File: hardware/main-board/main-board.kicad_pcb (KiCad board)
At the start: 2 copper layers, 176 x 55 mm, 101 parts, among them J1 BARREL_JACK, J2 CONN_01X10, J3 CONN_01X10, J4 USB_OTG, J5 CONN_02X05, J6 SMA, Q1 DDTD113ZC, Q2 DDTD113ZC, Q3 DDTD113ZC, Q4 DDTD113ZC, Q5 DDTD113ZC, Q6 FDB14N30TM, Q7 DDTD113ZC, Q8 DDTD113ZC, Q9 DDTD113ZC, SW1 SW_Push, SW2 SW_Push, SW3 SW_Push, SW4 SW_Push, SW5 SW_DIP_x01, U1 LD1117S33TR, U2 MAX1771, U3 STM32F302C, U4 FGPMMOPA6H, Y1 8MHz, Y2 32.768kHz

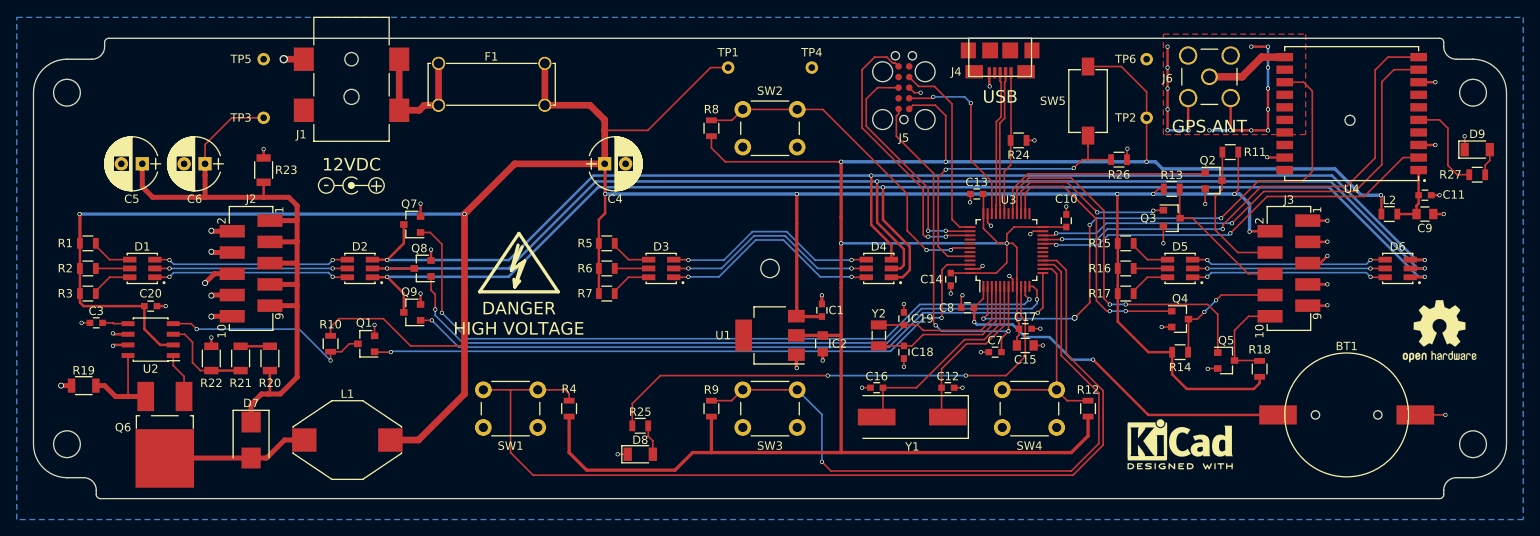
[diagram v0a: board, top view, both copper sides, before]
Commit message: Fixed HV5522 footprint on tube board.  Increased size of IN-14 through holes.  Fixed footprint for MOSFET in HV boost circuit.  Fixed hole size for battery holder footprint.
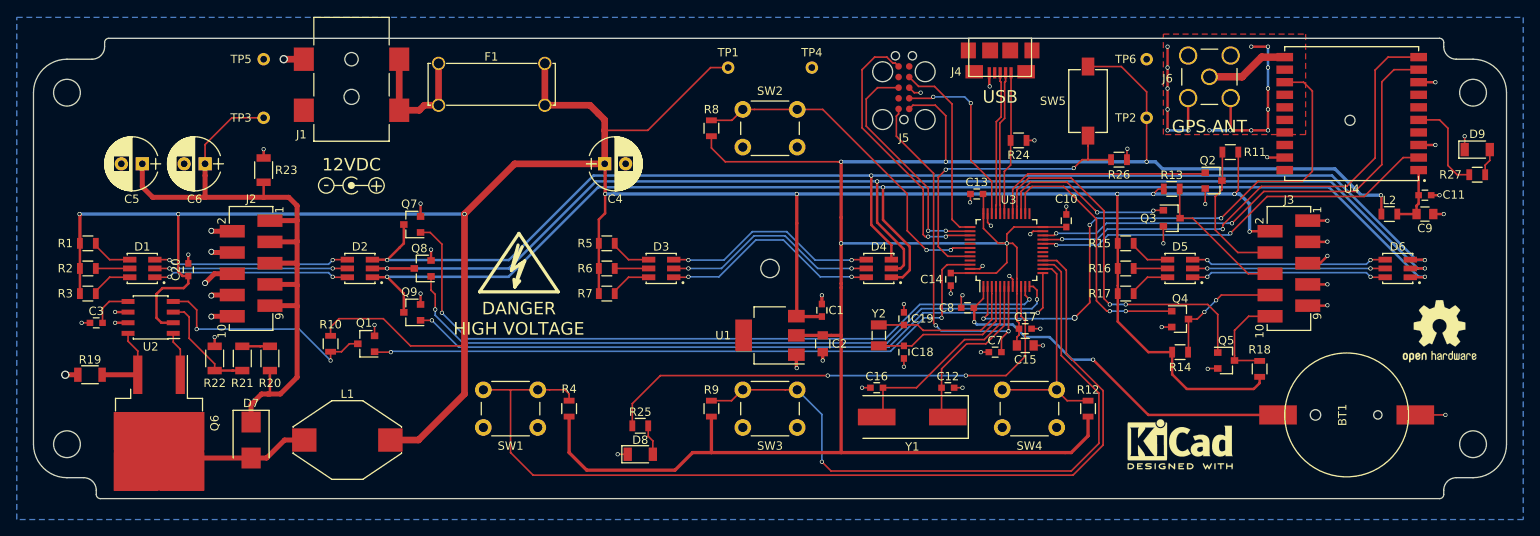
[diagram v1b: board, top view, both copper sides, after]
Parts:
- Q6: footprint TO_SOT_Packages_SMD:TO-252-2Lead -> TO_SOT_Packages_SMD:TO-263-2
- moved C20 6.26 mm to (80.5, 90.2), turned to 90 degrees
- moved U2 2.65 mm to (76.0, 95.8)
- moved R19 1.50 mm to (68.8, 102.7)
- moved Q6 0.88 mm to (77.0, 108.5)
- moved R22 0.40 mm to (83.7, 100.8)
- moved R21 0.20 mm to (87.0, 100.8)
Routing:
- net +12V: track 339.7 -> 342.4 mm, vias 8 -> 9
- net Net-(Q1-Pad3): track 25.3 -> 27.8 mm
- net Net-(C3-Pad1): track 3.09 -> 5.13 mm
- net Net-(R21-Pad2): track 11.3 -> 13.1 mm
- net Net-(Q6-Pad3): track 11.4 -> 9.69 mm
- net Net-(D7-Pad2): track 17.6 -> 16.1 mm

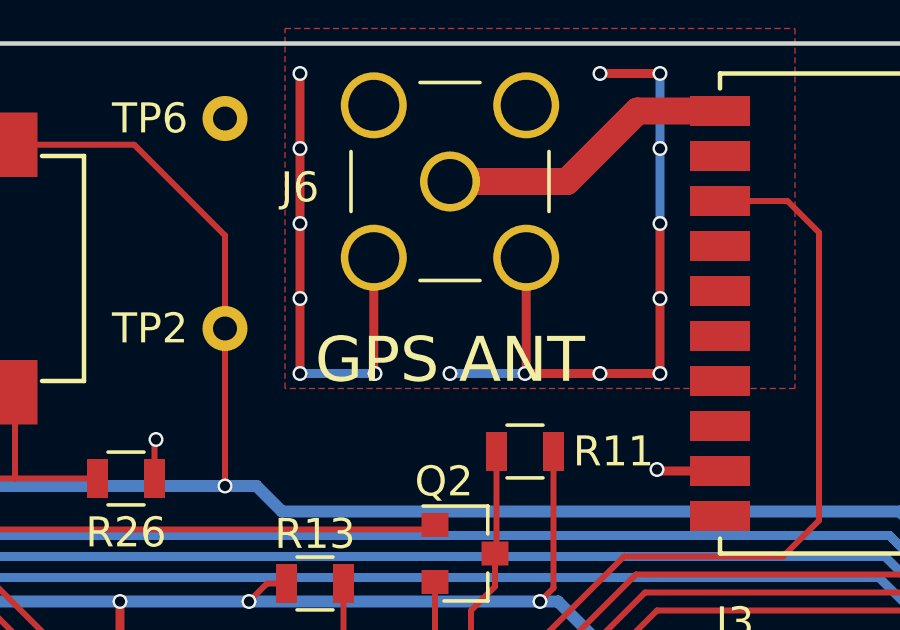
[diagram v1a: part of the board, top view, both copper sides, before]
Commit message: Modified thermal relief on SMA connector
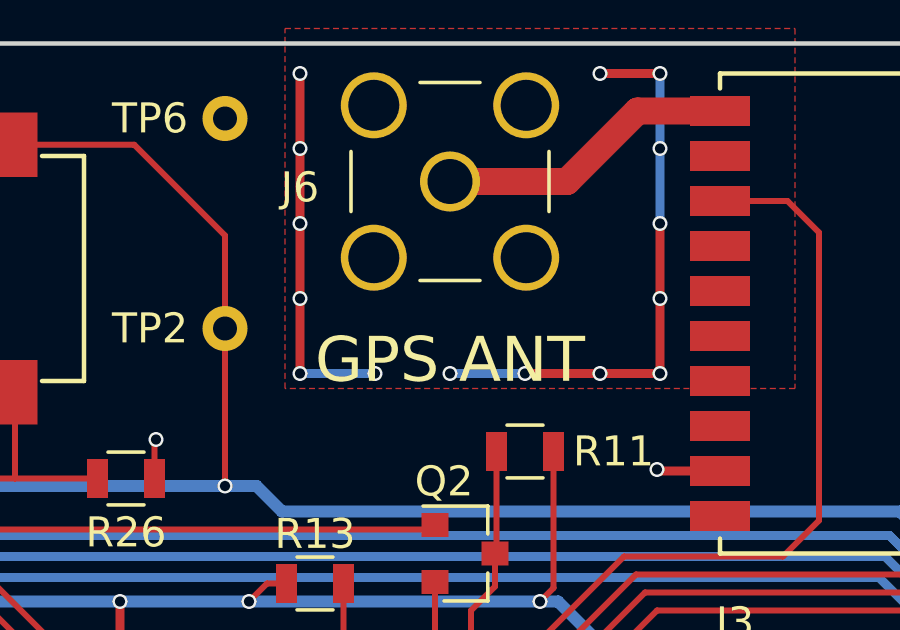
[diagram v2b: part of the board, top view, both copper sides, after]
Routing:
- net GND: track 130.1 -> 122.4 mm
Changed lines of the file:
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@@
     (thickness 1.6)
     (drawings 34)
-    (tracks 950)
+    (tracks 948)
     (zones 0)
     (modules 101)
@@
     (user_trace_width 0.8)
     (trace_clearance 0.2)
-    (zone_clearance 0.5)
+    (zone_clearance 0.16)
     (zone_45_only no)
     (trace_min 0.16)
@@
   (segment (start 205 73.5) (end 202.5 73.5) (width 0.3) (layer B.Cu) (net 1))
   (via (at 202.5 73.5) (size 0.5) (drill 0.34) (layers F.Cu B.Cu) (net 1))
-  (segment (start 205.04 69.64) (end 205.04 73.46) (width 0.3) (layer F.Cu) (net 1))
   (segment (start 205.04 73.46) (end 205 73.5) (width 0.3) (layer F.Cu) (net 1))
   (via (at 205 73.5) (size 0.5) (drill 0.34) (layers F.Cu B.Cu) (net 1))
-  (segment (start 199.96 69.64) (end 199.96 73.46) (width 0.3) (layer F.Cu) (net 1))
   (segment (start 199.96 73.46) (end 200 73.5) (width 0.3) (layer F.Cu) (net 1))
   (via (at 200 73.5) (size 0.5) (drill 0.34) (layers F.Cu B.Cu) (net 1))
@@
     (connect_pads (clearance 0.16))
     (min_thickness 0.2)
-    (fill yes (arc_segments 16) (thermal_gap 0.22) (thermal_bridge_width 0.4) (smoothing fillet) (radius 0.5))
+    (fill yes (arc_segments 16) (thermal_gap 0.4) (thermal_bridge_width 0.3) (smoothing fillet) (radius 0.2))
     (polygon
       (pts

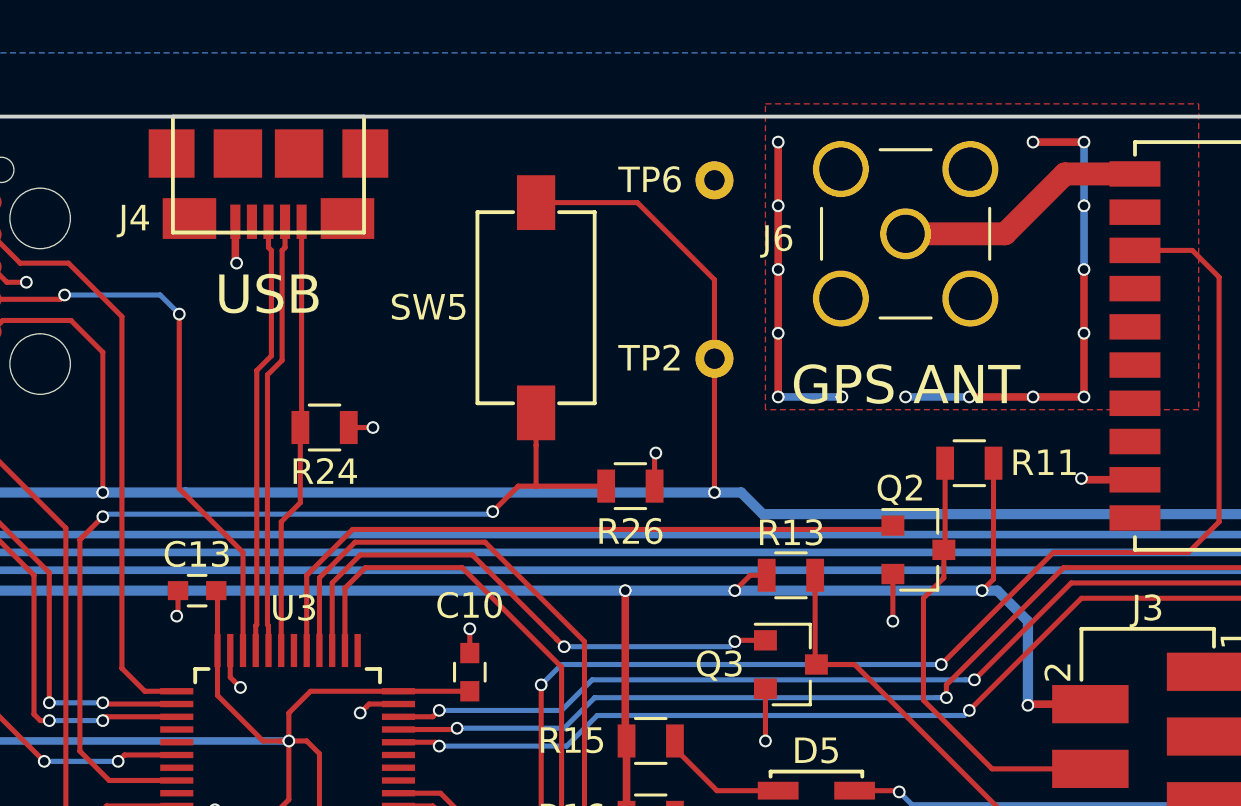
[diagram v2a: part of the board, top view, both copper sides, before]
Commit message: Added pull up circuit for USB.  Changed boot switch to a right angle pushbutton so that it can be used to switch to bootloader mode within the enclosure
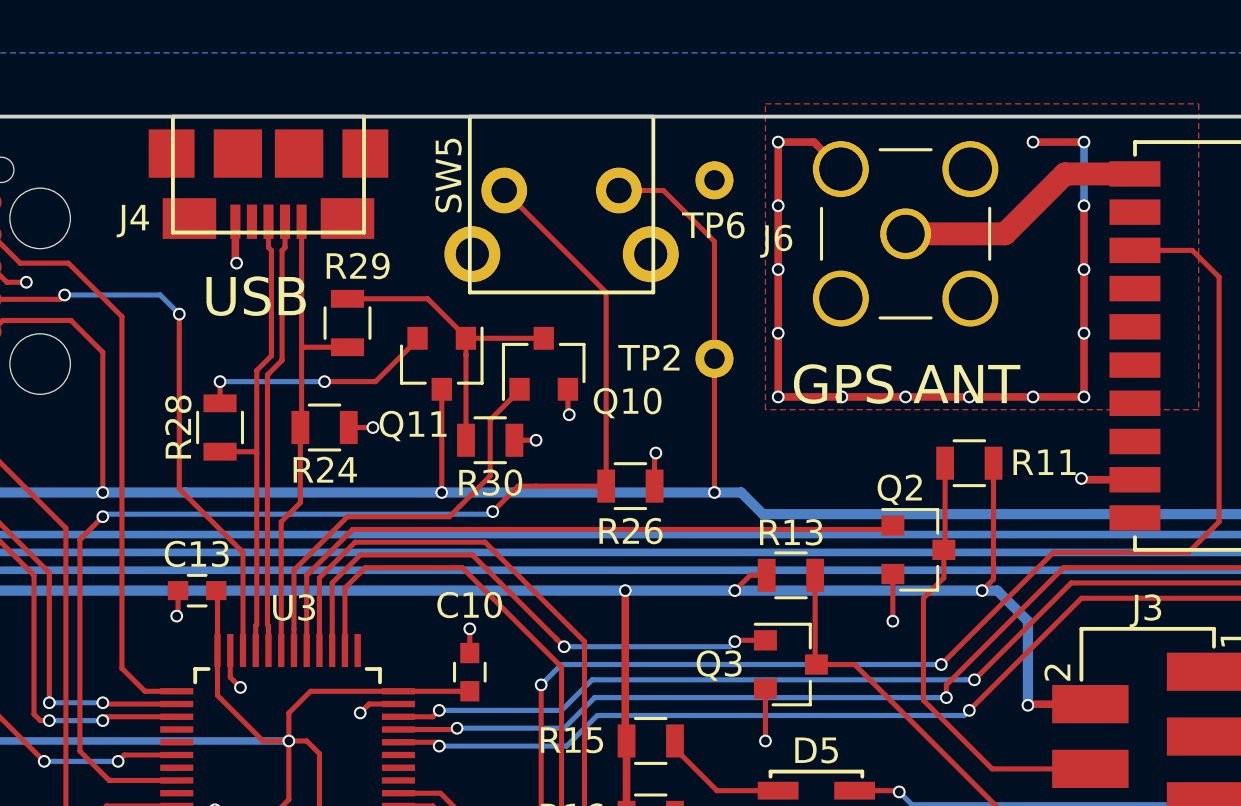
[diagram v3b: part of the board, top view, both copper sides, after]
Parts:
- added Q10: DDTD113ZC, TO_SOT_Packages_SMD:SOT-23, F.Cu at (188.3, 72.2)
- added Q11: MMBT2222A, TO_SOT_Packages_SMD:SOT-23, F.Cu at (184.3, 72.2)
- added R28: 1.5k, Resistors_SMD:R_0805, F.Cu at (175.6, 74.7)
- added R29: 10k, Resistors_SMD:R_0805, F.Cu at (180.6, 70.6)
- added R30: 36.5k, Resistors_SMD:R_0805, F.Cu at (186.2, 75.2)
- R23: value 254k -> 255k
- R25, R27: value R -> 274
- SW5: value SW_DIP_x01 -> SW_Push; footprint radio-clock:SDA01H1SBD -> radio-clock:TL1105SF160Q
- moved SW5 7.57 mm to (189.0, 62.5), turned to 180 degrees
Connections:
- U3 pad 30: Net-(U3-Pad30) -> /USB_DISCONN
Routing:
- net /USB_DISCONN: track 0.00 -> 16.3 mm
- net Net-(Q10-Pad3): track 0.00 -> 12.4 mm
- net /BOOT0: track 37.0 -> 47.4 mm
- net Net-(Q11-Pad2): track 0.00 -> 9.33 mm, vias 0 -> 2
- net GND: track 122.4 -> 129.6 mm, vias 71 -> 73
- net +3V3: track 287.6 -> 289.5 mm, vias 6 -> 7
- net /USB_VBUS: track 17.2 -> 19.0 mm
- net /USB_D+: track 17.1 -> 18.6 mm
